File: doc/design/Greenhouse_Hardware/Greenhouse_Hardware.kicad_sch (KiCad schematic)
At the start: 4 parts, among them J1 M5Stack Watering Unit U101, J2 SSD1306 OLED Module, J3 DHT11 module, U1 ESP32-DevKitC

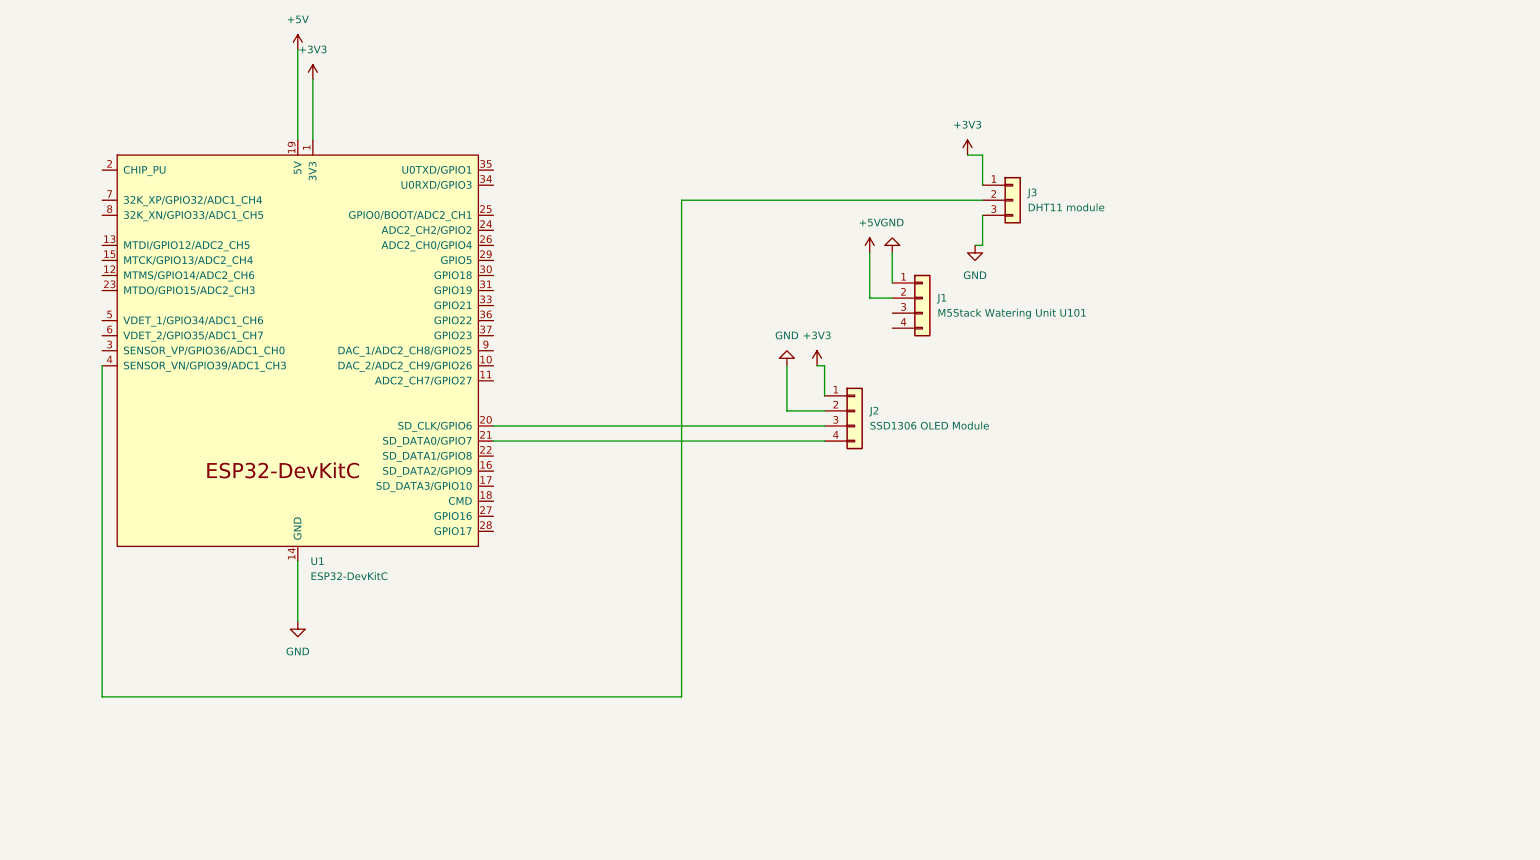
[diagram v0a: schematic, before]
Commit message: Added a temp/humid functionality and light detection, have to fix the oposite resistance of the photoresistor and display the actual lux
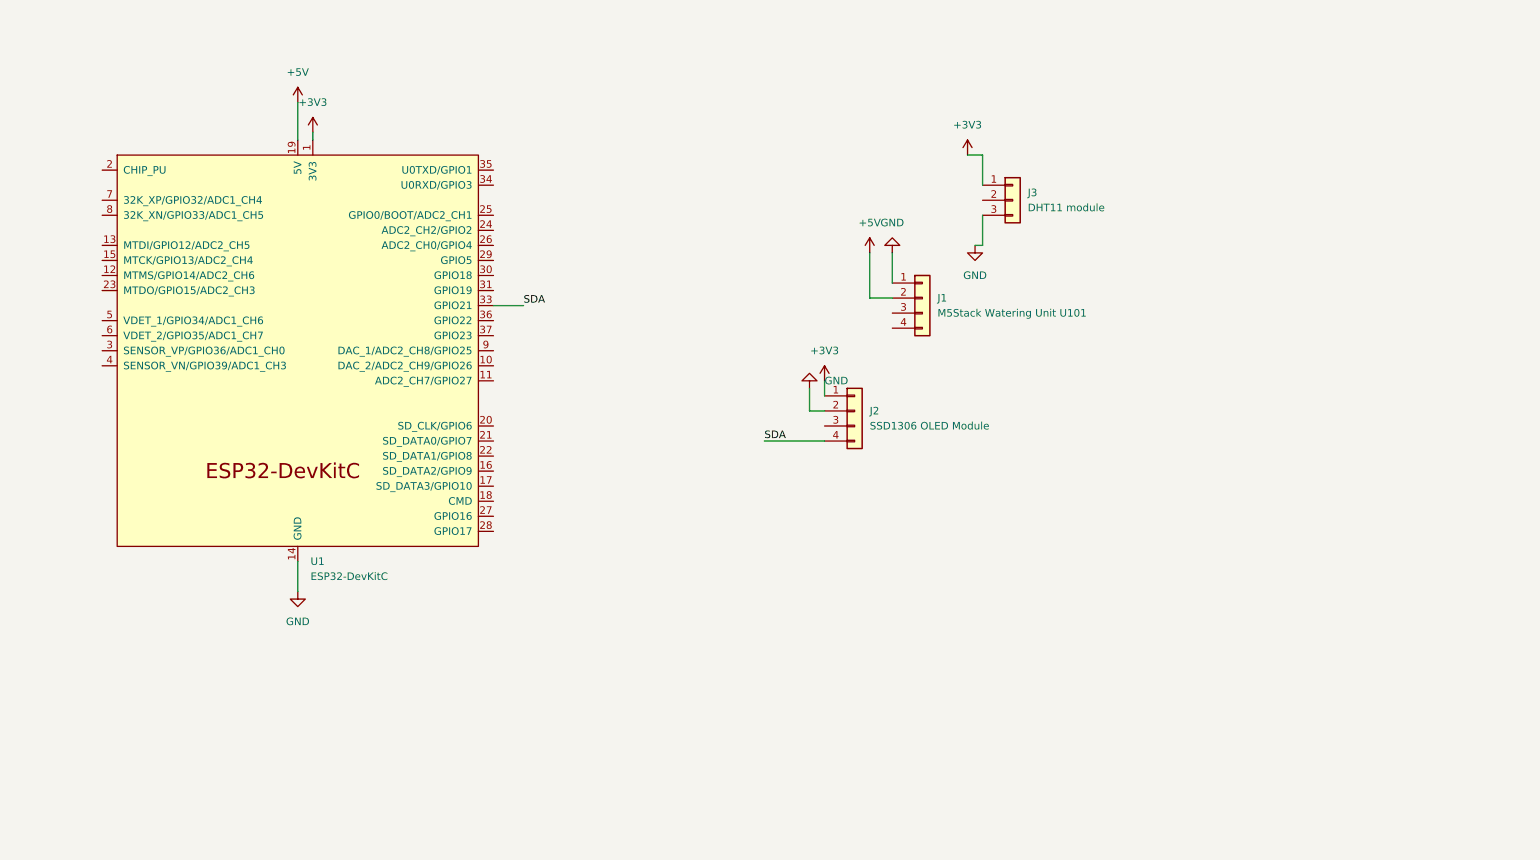
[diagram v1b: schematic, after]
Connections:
- net at U1.20 (SD_CLK/GPIO6): no longer J2.3 (Pin_3)
- net at U1.21 (SD_DATA0/GPIO7): no longer J2.4 (Pin_4)
- net SDA: now reaches U1.33 (GPIO21)
- net SDA: now also J2.4 (Pin_4)
- net at U1.4 (SENSOR_VN/GPIO39/ADC1_CH3): no longer J3.2 (Pin_2)
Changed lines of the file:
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@@
 	(wire
 		(pts
-			(xy 63.5 105.41) (xy 63.5 115.57)
+			(xy 63.5 105.41) (xy 63.5 110.49)
 		)
 		(stroke
@@
 	(wire
 		(pts
+			(xy 96.52 62.23) (xy 101.6 62.23)
+		)
+		(stroke
+			(width 0)
+			(type default)
+		)
+	)
+	(wire
+		(pts
+			(xy 149.86 76.2) (xy 149.86 80.01)
+		)
+		(stroke
+			(width 0)
+			(type default)
+		)
+	)
+	(wire
+		(pts
 			(xy 179.07 36.83) (xy 176.53 36.83)
 		)
@@
 	(wire
 		(pts
-			(xy 128.27 128.27) (xy 30.48 128.27)
-		)
-		(stroke
-			(width 0)
-			(type default)
-		)
-	)
-	(wire
-		(pts
-			(xy 30.48 128.27) (xy 30.48 72.39)
-		)
-		(stroke
-			(width 0)
-			(type default)
-		)
-	)
-	(wire
-		(pts
-			(xy 146.05 80.01) (xy 146.05 72.39)
-		)
-		(stroke
-			(width 0)
-			(type default)
-		)
-	)
-	(wire
-		(pts
-			(xy 152.4 77.47) (xy 152.4 72.39)
-		)
-		(stroke
-			(width 0)
-			(type default)
-		)
-	)
-	(wire
-		(pts
-			(xy 63.5 19.05) (xy 63.5 34.29)
-		)
-		(stroke
-			(width 0)
-			(type default)
-		)
-	)
-	(wire
-		(pts
-			(xy 152.4 82.55) (xy 96.52 82.55)
-		)
-		(stroke
-			(width 0)
-			(type default)
-		)
-	)
-	(wire
-		(pts
-			(xy 179.07 44.45) (xy 128.27 44.45)
-		)
-		(stroke
-			(width 0)
-			(type default)
-		)
-	)
-	(wire
-		(pts
-			(xy 152.4 72.39) (xy 151.13 72.39)
+			(xy 142.24 85.09) (xy 152.4 85.09)
+		)
+		(stroke
+			(width 0)
+			(type default)
+		)
+	)
+	(wire
+		(pts
+			(xy 63.5 27.94) (xy 63.5 34.29)
 		)
 		(stroke
@@
 	(wire
 		(pts
-			(xy 152.4 80.01) (xy 146.05 80.01)
-		)
-		(stroke
-			(width 0)
-			(type default)
-		)
-	)
-	(wire
-		(pts
-			(xy 66.04 24.13) (xy 66.04 34.29)
-		)
-		(stroke
-			(width 0)
-			(type default)
-		)
-	)
-	(wire
-		(pts
-			(xy 128.27 44.45) (xy 128.27 128.27)
+			(xy 66.04 33.02) (xy 66.04 34.29)
 		)
 		(stroke
@@
 	(wire
 		(pts
-			(xy 152.4 85.09) (xy 96.52 85.09)
+			(xy 149.86 80.01) (xy 152.4 80.01)
+		)
+		(stroke
+			(width 0)
+			(type default)
+		)
+	)
+	(wire
+		(pts
+			(xy 152.4 74.93) (xy 152.4 77.47)
 		)
 		(stroke
@@
 			(width 0)
 			(type default)
+		)
+	)
+	(label "SDA"
+		(at 101.6 62.23 0)
+		(effects
+			(font
+				(size 1.27 1.27)
+			)
+			(justify left bottom)
+		)
+	)
+	(label "SDA"
+		(at 142.24 85.09 0)
+		(effects
+			(font
+				(size 1.27 1.27)
+			)
+			(justify left bottom)
 		)
 	)
 	(symbol
 		(lib_id "power:GND")
-		(at 63.5 115.57 0)
+		(at 63.5 110.49 0)
 		(unit 1)
 		(body_style 1)
@@
 		(fields_autoplaced yes)
 		(property "Reference" "#PWR01"
-			(at 63.5 121.92 0)
+			(at 63.5 116.84 0)
 			(hide yes)
 			(show_name no)
@@
 		)
 		(property "Value" "GND"
-			(at 63.5 120.65 0)
+			(at 63.5 115.57 0)
 			(show_name no)
 			(do_not_autoplace no)
@@
 		)
 		(property "Footprint" "PCM_Espressif:ESP32-DevKitC"
-			(at 63.5 115.57 0)
+			(at 63.5 110.49 0)
 			(hide yes)
 			(show_name no)
@@
 		)
 		(property "Datasheet" ""
-			(at 63.5 115.57 0)
+			(at 63.5 110.49 0)
 			(hide yes)
 			(show_name no)
@@
 		)
 		(property "Description" "Power symbol creates a global label with name \"GND\" , ground"
-			(at 63.5 115.57 0)
+			(at 63.5 110.49 0)
 			(hide yes)
 			(show_name no)
@@
 	(symbol
 		(lib_id "power:+3V3")
-		(at 66.04 24.13 0)
+		(at 66.04 33.02 0)
 		(unit 1)
 		(body_style 1)
@@
 		(fields_autoplaced yes)
 		(property "Reference" "#PWR02"
+			(at 66.04 36.83 0)
+			(hide yes)
+			(show_name no)
+			(do_not_autoplace no)
+			(effects
+				(font
+					(size 1.27 1.27)
+				)
+			)
+		)
+		(property "Value" "+3V3"
 			(at 66.04 27.94 0)
-			(hide yes)
-			(show_name no)
-			(do_not_autoplace no)
-			(effects
-				(font
-					(size 1.27 1.27)
-				)
-			)
-		)
-		(property "Value" "+3V3"
-			(at 66.04 19.05 0)
 			(show_name no)
 			(do_not_autoplace no)
@@
 		)
 		(property "Footprint" "Package_DFN_QFN:Diodes_UDFN3810-9_TYPE_B"
-			(at 66.04 24.13 0)
+			(at 66.04 33.02 0)
 			(hide yes)
 			(show_name no)
@@
 		)
 		(property "Datasheet" ""
-			(at 66.04 24.13 0)
+			(at 66.04 33.02 0)
 			(hide yes)
 			(show_name no)
@@
 		)
 		(property "Description" "Power symbol creates a global label with name \"+3V3\""
-			(at 66.04 24.13 0)
+			(at 66.04 33.02 0)
 			(hide yes)
 			(show_name no)
@@
 	(symbol
 		(lib_id "power:GND")
-		(at 146.05 72.39 180)
+		(at 149.86 76.2 180)
 		(unit 1)
 		(body_style 1)
@@
 		(fields_autoplaced yes)
 		(property "Reference" "#PWR07"
-			(at 146.05 66.04 0)
+			(at 149.86 69.85 0)
 			(hide yes)
 			(show_name no)
@@
 		)
 		(property "Value" "GND"
-			(at 146.05 67.31 0)
-			(show_name no)
-			(do_not_autoplace no)
-			(effects
-				(font
-					(size 1.27 1.27)
-				)
+			(at 152.4 74.9299 0)
+			(show_name no)
+			(do_not_autoplace no)
+			(effects
+				(font
+					(size 1.27 1.27)
+				)
+				(justify right)
 			)
 		)
 		(property "Footprint" ""
-			(at 146.05 72.39 0)
+			(at 149.86 76.2 0)
 			(hide yes)
 			(show_name no)
@@
 		)
 		(property "Datasheet" ""
-			(at 146.05 72.39 0)
+			(at 149.86 76.2 0)
 			(hide yes)
 			(show_name no)
@@
 		)
 		(property "Description" "Power symbol creates a global label with name \"GND\" , ground"
-			(at 146.05 72.39 0)
+			(at 149.86 76.2 0)
 			(hide yes)
 			(show_name no)
@@
 	(symbol
 		(lib_id "power:+5V")
-		(at 63.5 19.05 0)
+		(at 63.5 27.94 0)
 		(unit 1)
 		(body_style 1)
@@
 		(fields_autoplaced yes)
 		(property "Reference" "#PWR06"
+			(at 63.5 31.75 0)
+			(hide yes)
+			(show_name no)
+			(do_not_autoplace no)
+			(effects
+				(font
+					(size 1.27 1.27)
+				)
+			)
+		)
+		(property "Value" "+5V"
 			(at 63.5 22.86 0)
-			(hide yes)
-			(show_name no)
-			(do_not_autoplace no)
-			(effects
-				(font
-					(size 1.27 1.27)
-				)
-			)
-		)
-		(property "Value" "+5V"
-			(at 63.5 13.97 0)
 			(show_name no)
 			(do_not_autoplace no)
@@
 		)
 		(property "Footprint" ""
-			(at 63.5 19.05 0)
+			(at 63.5 27.94 0)
 			(hide yes)
 			(show_name no)
@@
 		)
 		(property "Datasheet" ""
-			(at 63.5 19.05 0)
+			(at 63.5 27.94 0)
 			(hide yes)
 			(show_name no)
@@
 		)
 		(property "Description" "Power symbol creates a global label with name \"+5V\""
-			(at 63.5 19.05 0)
+			(at 63.5 27.94 0)
 			(hide yes)
 			(show_name no)
@@
 	(symbol
 		(lib_id "power:+3V3")
-		(at 151.13 72.39 0)
+		(at 152.4 74.93 0)
 		(unit 1)
 		(body_style 1)
@@
 		(fields_autoplaced yes)
 		(property "Reference" "#PWR04"
-			(at 151.13 76.2 0)
+			(at 152.4 78.74 0)
 			(hide yes)
 			(show_name no)
@@
 		)
 		(property "Value" "+3V3"
-			(at 151.13 67.31 0)
+			(at 152.4 69.85 0)
 			(show_name no)
 			(do_not_autoplace no)
@@
 		)
 		(property "Footprint" ""
-			(at 151.13 72.39 0)
+			(at 152.4 74.93 0)
 			(hide yes)
 			(show_name no)
@@
 		)
 		(property "Datasheet" ""
-			(at 151.13 72.39 0)
+			(at 152.4 74.93 0)
 			(hide yes)
 			(show_name no)
@@
 		)
 		(property "Description" "Power symbol creates a global label with name \"+3V3\""
-			(at 151.13 72.39 0)
-			(hide yes)
-			(show_name no)
+			(at 152.4 74.93 0)
+			(hide yes)
+			(show_name no)

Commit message: WiFi functionallity and sensor reading, validation, data display
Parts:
- added J4: K-0135 Water Level Sensor, symbol Connector_Generic:Conn_01x03
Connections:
- net +3V3: now also J4.2 (Pin_2)
- net GND: now also J4.1 (Pin_1)
- net at J1.4 (Pin_4): now also U1.8 (32K_XN/GPIO33/ADC1_CH5)
- net at U1.28 (GPIO17): now also J3.2 (Pin_2)
- net at U1.36 (GPIO22): now also J2.3 (Pin_3)
- net at U1.6 (VDET_2/GPIO35/ADC1_CH7): now also J4.3 (Pin_3)
- net SDA: no longer names the net of J2.4 (Pin_4), U1.33 (GPIO21)
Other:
- moved on the sheet: J3

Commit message: finished analysis, advice, design, realization. WOrking on the verification and validation, which is also almost finished. Didnt upload for a week, because i forgor
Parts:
- added J5: Photoresistor + LM393, symbol Connector_Generic:Conn_01x04
- added J6: Regulated 5V 2.5A DC supply, symbol Connector_Generic:Conn_01x02
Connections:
- net +3V3: now also J5.1 (Pin_1)
- net +5V: now also J6.2 (Pin_2); no longer U1.19 (5V)
- net GND: now also J5.2 (Pin_2), J6.1 (Pin_1)
- net at J1.3 (Pin_3): now also U1.27 (GPIO16)
- net at U1.5 (VDET_1/GPIO34/ADC1_CH6): now also J5.4 (Pin_4)
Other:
- moved on the sheet: J1, J2, J3, J4, U1
